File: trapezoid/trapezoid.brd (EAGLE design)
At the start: 90 x 35 mm, 29 parts, among them IC2 LGD20H, U1 MMA8452Q, U2 microSD, U3 DS3234, U4 MCP73831

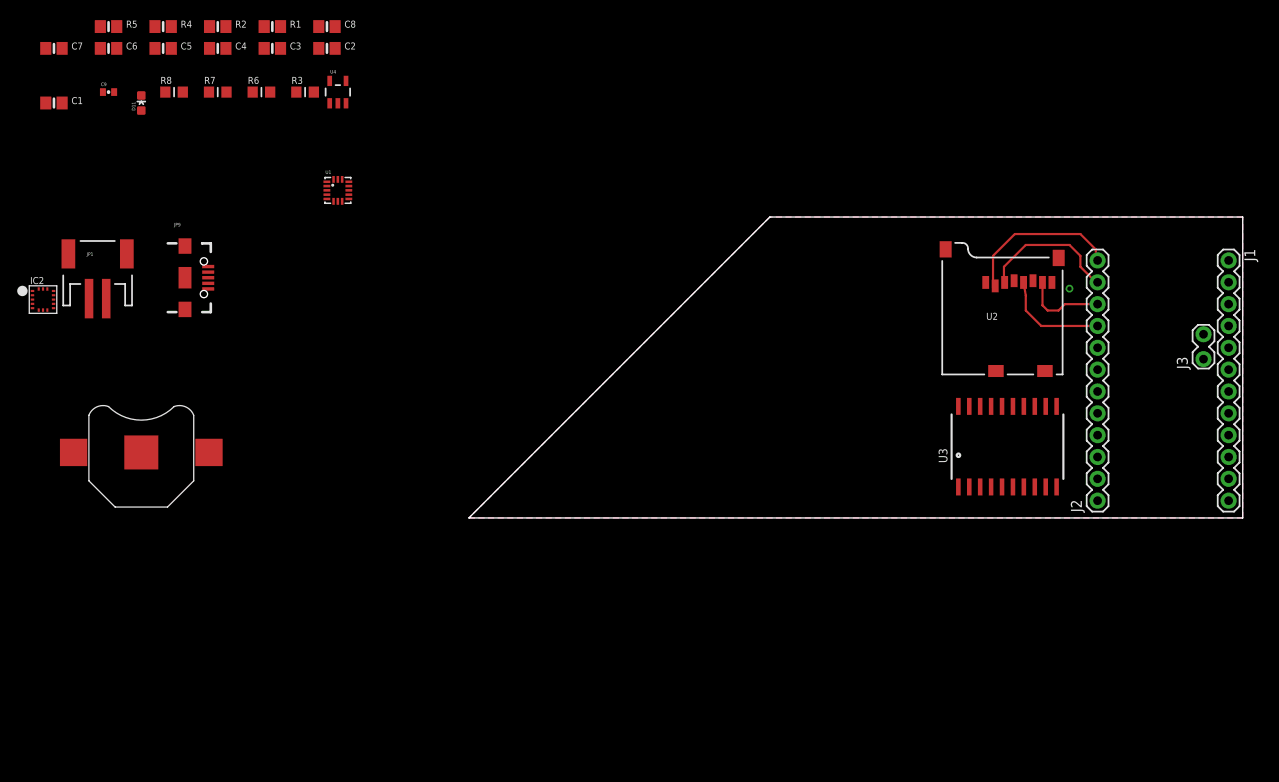
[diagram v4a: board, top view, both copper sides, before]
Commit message: chnaged rtc to ds1339b in trap
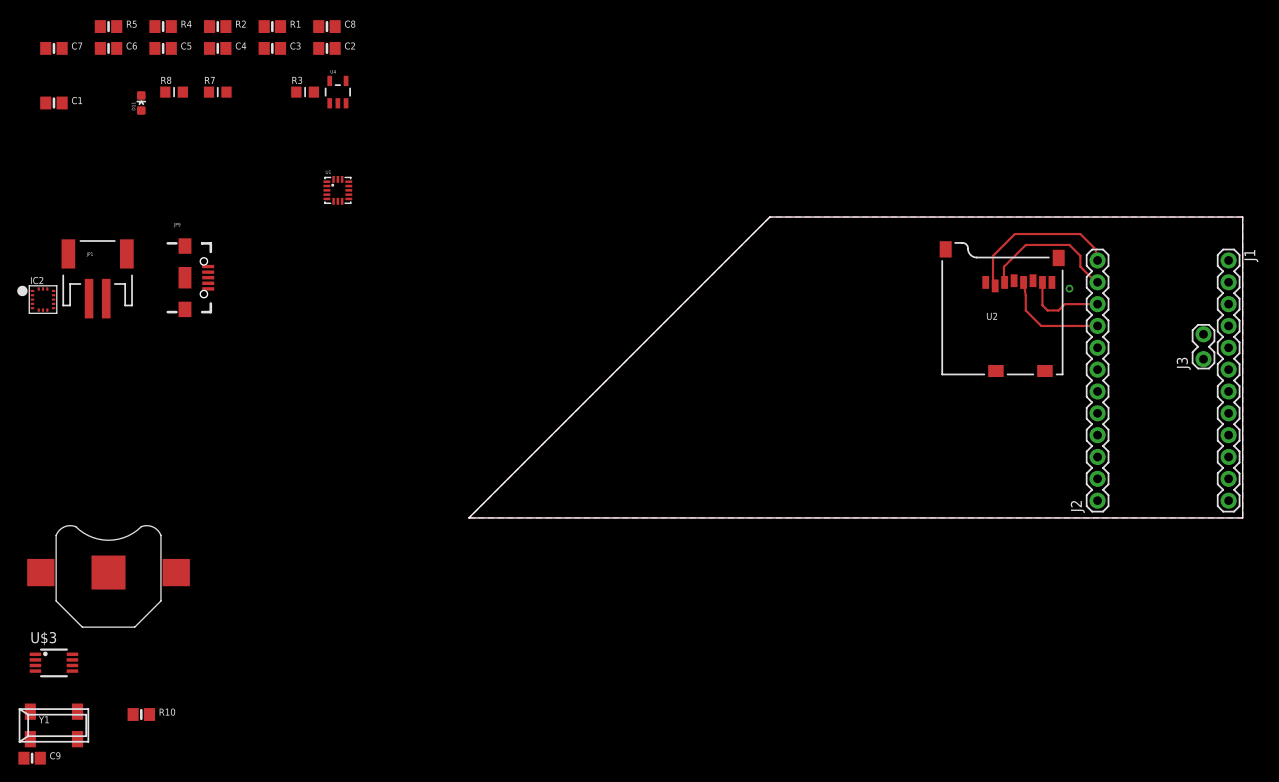
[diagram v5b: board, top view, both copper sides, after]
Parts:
- removed R6: 10K, microbuilder:_0805MP
- removed U3: DS3234, SparkFun:DS3234
- added R10: 10K, microbuilder:0805-NO
- added U$3: DS1339BDS1339B, sharkdunio:8U-SOP
- added Y1: CRYSTAL.ABS25, abracon:ABS25
- C9: value 22pF -> 0.1uF; device SparkFun:0402-CAP -> microbuilder:0805-NO
- moved C9 78.0 mm to (-50.8, -27.9)
- moved BAT1 14.5 mm to (-41.9, -6.35)
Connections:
- removed net INT/SQW: J1.8, U3.5
- removed net RTCBATT: BAT1.PWR@1, U3.16
- new net N$2: U$3.2, Y1.4
- new net N$4: BAT1.PWR@1, U$3.3
- new net N$5: U$3.1, Y1.1
- new net SQW/INT: J1.8, R10.1, U$3.7
- net +3V3: now also C9.2, R10.2, U$3.8; no longer C9.1, R6.2, U3.4
- net GND: now also C9.1, U$3.4; no longer C9.2, U3.10, U3.11, U3.12, U3.13, U3.14, U3.15, U3.2, U3.7, U3.8, U3.9
- net MISO: no longer U3.19
- net MOSI: no longer U3.17
- net RTC_CS: no longer U3.1
- net SCK: no longer U3.18, U3.20
- net SCL: now also U$3.6
- net SDA: now also U$3.5

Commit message: rotated pro mini
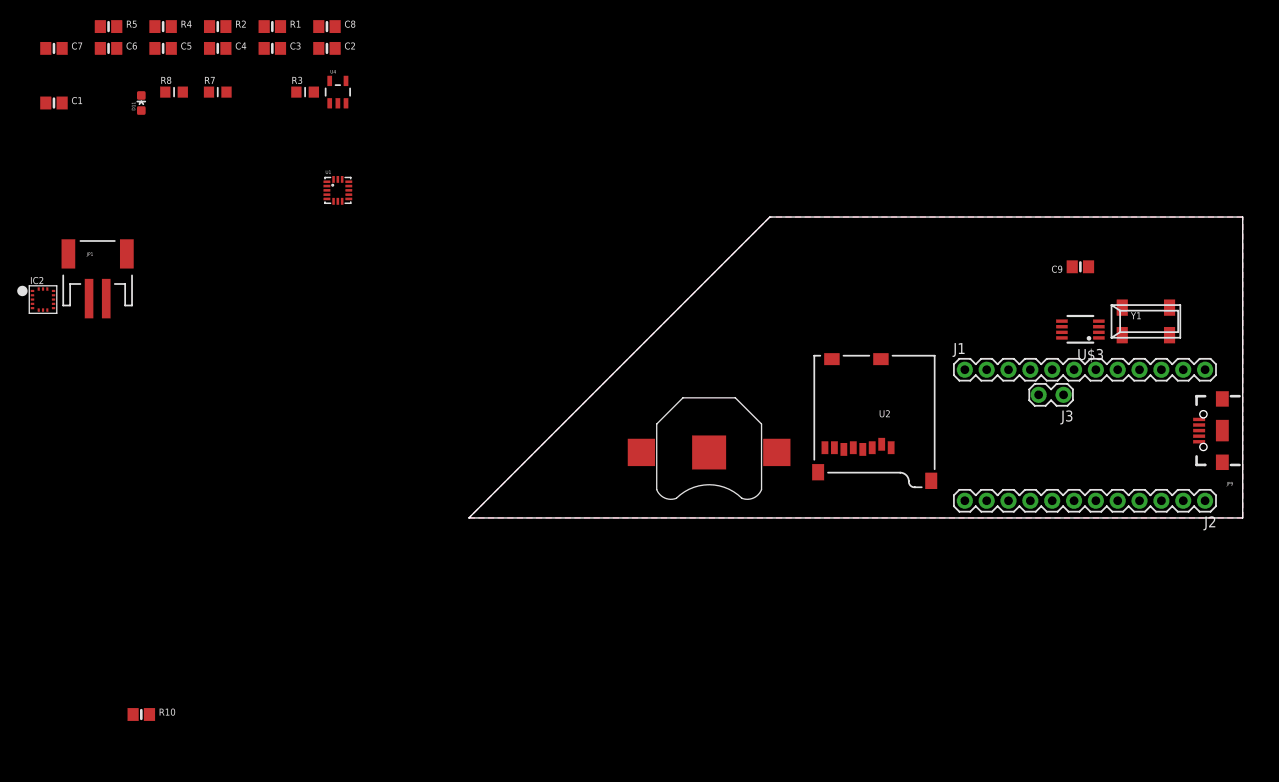
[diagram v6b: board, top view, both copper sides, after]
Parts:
- moved Y1 135.4 mm to (78.7, 22.9)
- moved C9 134.6 mm to (71.1, 29.2), turned to 180 degrees
- moved U$3 125.3 mm to (71.1, 21.6), turned to 180 degrees
- moved JP9 122.0 mm to (87.6, 10.2), turned to 180 degrees
- moved BAT1 71.2 mm to (27.9, 7.62), turned to 180 degrees
- moved J1 33.2 mm to (57.7, 17.2), turned to 0 degrees
- moved U2 29.0 mm to (40.2, 18.9), turned to 180 degrees
- moved J3 17.0 mm to (69.0, 14.3), turned to 180 degrees
- moved J2 12.5 mm to (85.6, 2.00), turned to 180 degrees
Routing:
- net SD_CS: track 19.4 -> 0.20 mm
- net MOSI: track 16.3 -> 0.00 mm
- net SCK: track 12.4 -> 0.00 mm
- net MISO: track 9.63 -> 0.00 mm

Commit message: placed rtc and usd
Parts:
- moved JP1 128.2 mm to (83.8, 11.4), flipped to the bottom, turned to 90 degrees
- moved R10 125.5 mm to (78.7, 22.9)
- moved IC2 119.1 mm to (68.6, 10.2)
- moved U4 103.5 mm to (85.1, 24.1), turned to 270 degrees
- moved U1 96.8 mm to (77.5, 10.2), turned to 270 degrees
- moved C2 70.8 mm to (49.5, 29.2)
- moved C5 70.8 mm to (30.5, 29.2)
- moved C8 70.8 mm to (49.5, 31.8)
- moved D11 70.8 mm to (27.9, 22.9)
- moved R3 70.8 mm to (47.0, 24.1)
- moved R4 70.8 mm to (30.5, 31.8)
- moved C1 70.8 mm to (17.8, 22.9)
- moved C3 70.8 mm to (43.2, 29.2)
- moved C4 70.8 mm to (36.8, 29.2)
- moved C6 70.8 mm to (24.1, 29.2)
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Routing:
- net N$4: track 0.00 -> 41.8 mm, vias 0 -> 2
- net +3V3: track 0.00 -> 38.3 mm
- net SCK: track 0.00 -> 30.1 mm
- net MISO: track 0.00 -> 25.5 mm, vias 0 -> 1
- net MOSI: track 0.00 -> 22.9 mm
- net V_RAW: track 0.00 -> 19.4 mm
- net SD_CS: track 0.20 -> 14.6 mm
- net SQW/INT: track 0.00 -> 6.23 mm
- net GND: track 0.00 -> 5.70 mm, vias 0 -> 1
- net N$5: track 0.00 -> 4.91 mm
- net N$2: track 0.00 -> 4.13 mm

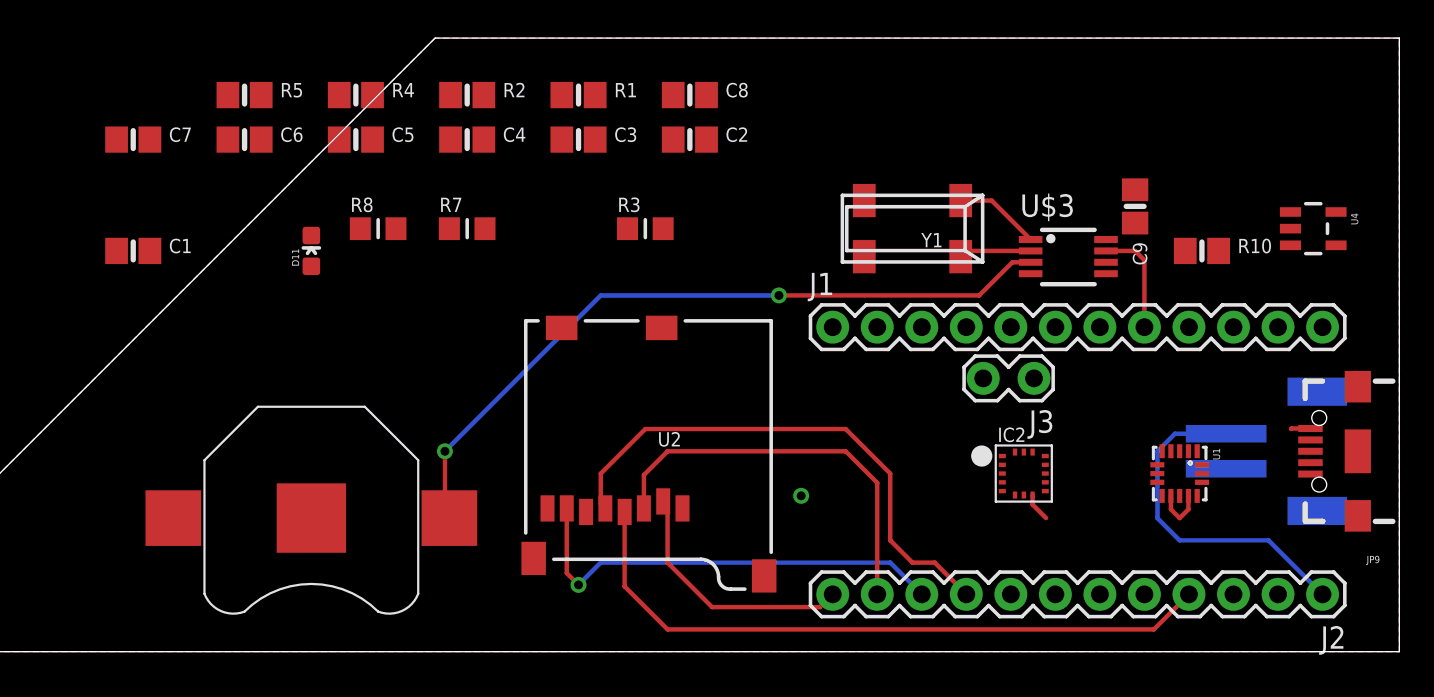
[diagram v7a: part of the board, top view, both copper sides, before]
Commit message: placed accel and gyro
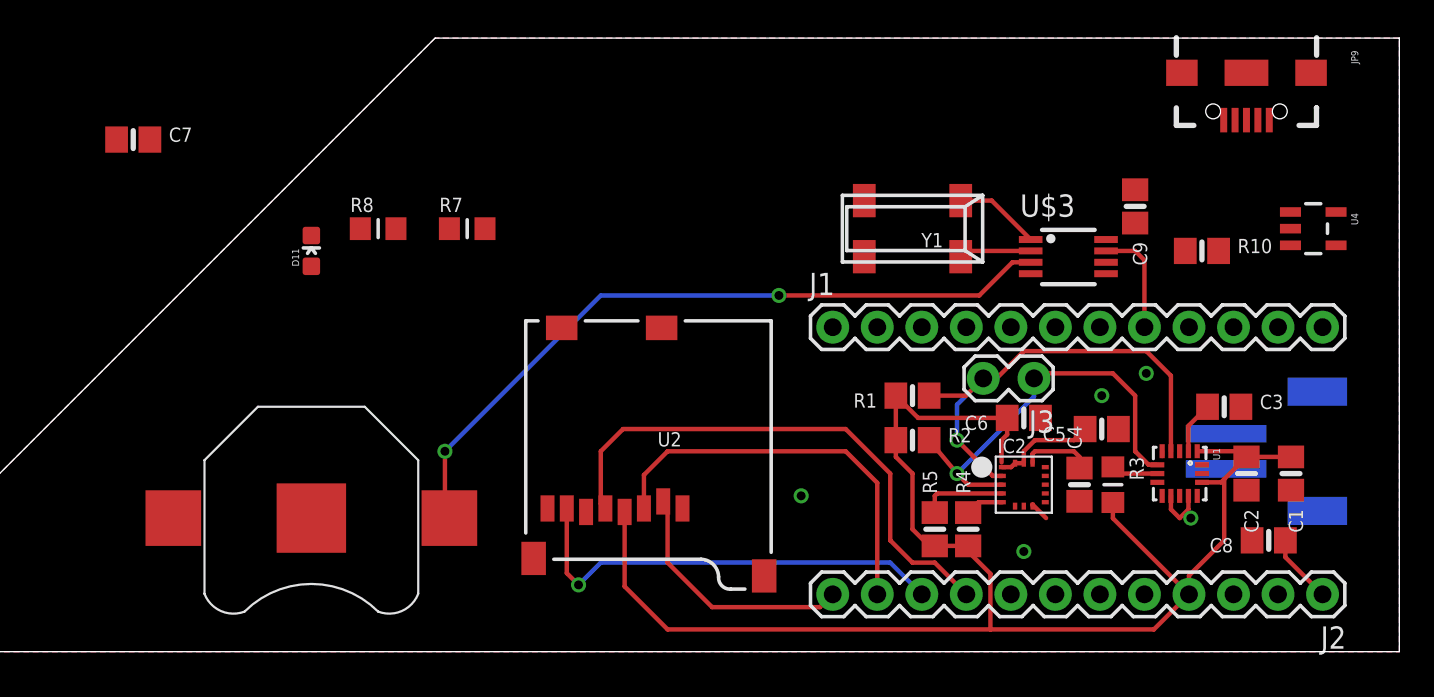
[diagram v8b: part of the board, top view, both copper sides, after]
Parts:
- moved C1 67.3 mm to (83.8, 10.2), turned to 270 degrees
- moved C6 47.2 mm to (68.6, 13.3), turned to 180 degrees
- moved R5 46.5 mm to (63.5, 6.99), turned to 90 degrees
- moved C5 45.6 mm to (73.0, 12.7), turned to 180 degrees
- moved R4 42.8 mm to (65.4, 6.99), turned to 90 degrees
- moved C8 41.7 mm to (82.5, 6.35), turned to 180 degrees
- moved C4 40.1 mm to (71.8, 9.53), turned to 90 degrees
- moved C3 39.9 mm to (80.0, 14.0)
- moved C2 37.0 mm to (81.3, 10.2), turned to 270 degrees
- moved R2 32.1 mm to (62.2, 12.1)
- moved R3 30.4 mm to (73.7, 9.53), turned to 270 degrees
- moved R1 25.6 mm to (62.2, 14.6), turned to 180 degrees
- moved JP9 22.5 mm to (81.3, 33.0), turned to 270 degrees
- moved IC2 0.63 mm to (68.6, 9.53)
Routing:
- net +3V3: track 38.3 -> 93.8 mm
- net SCL: track 0.00 -> 27.6 mm, vias 0 -> 1
- net SDA: track 0.00 -> 23.7 mm, vias 0 -> 1
- net V_RAW: track 19.4 -> 3.96 mm
- net SDO/SAO: track 0.00 -> 5.31 mm
- net N$3: track 0.00 -> 4.04 mm
- net BYP: track 0.00 -> 2.99 mm
- net SA0: track 0.00 -> 2.69 mm
- net CS_3.3V: track 0.00 -> 2.19 mm
- net GND: track 5.70 -> 4.40 mm, vias 1 -> 5
- net SCK: track 30.1 -> 30.9 mm
